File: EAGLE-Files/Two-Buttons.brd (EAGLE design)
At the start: 25.4 x 40.3 mm, 10 parts

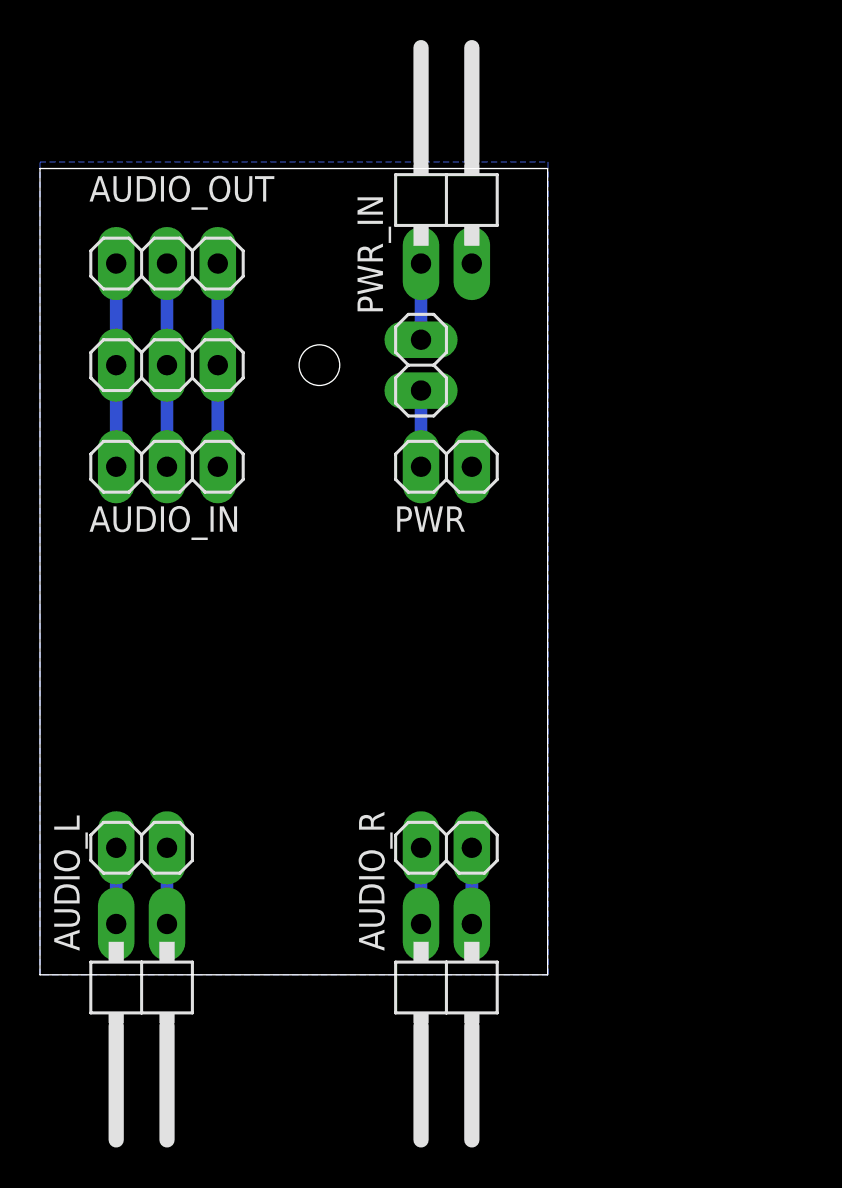
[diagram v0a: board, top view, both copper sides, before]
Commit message: Updated all boards for JLCPCB order
Also added the controller boards and schematics back
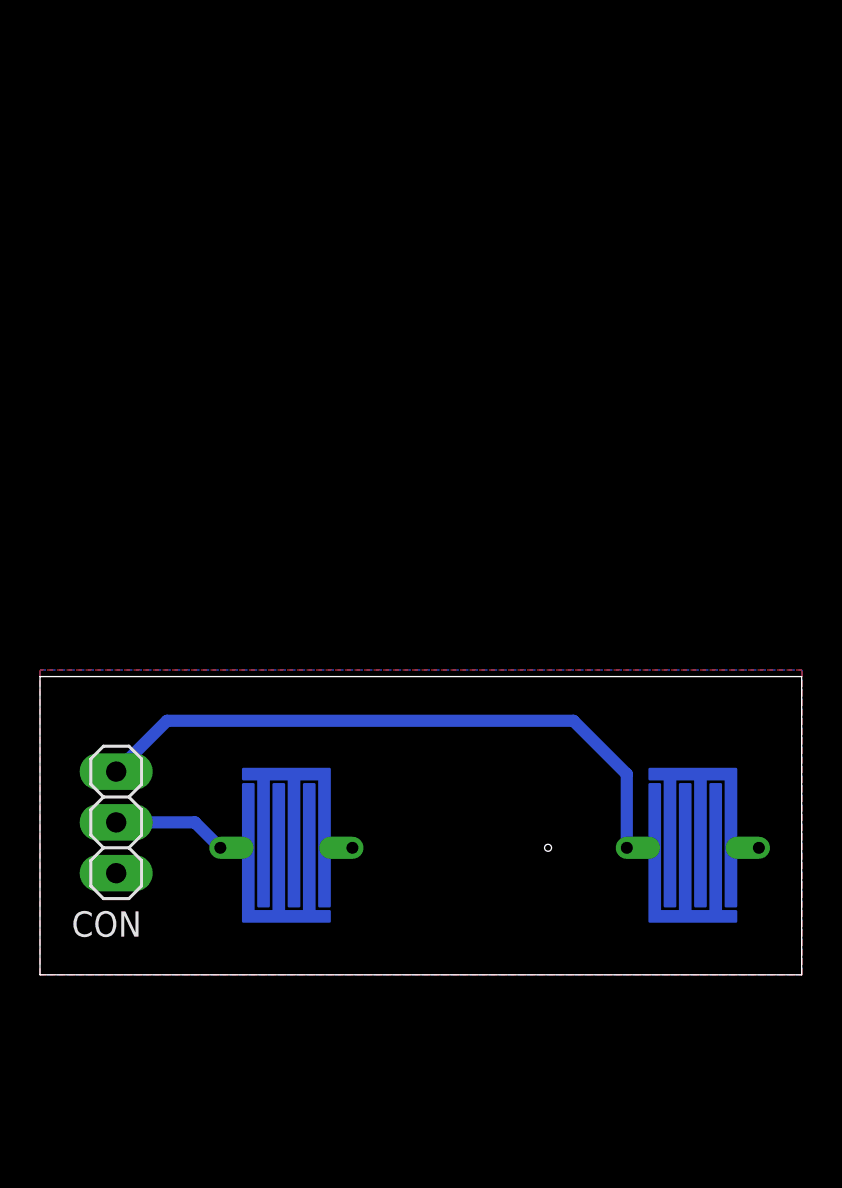
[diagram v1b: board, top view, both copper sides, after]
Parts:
- removed AUDIO_CONNECTOR, AUDIO_IN, AUDIO_OUT: (no value), pinhead:1X03
- removed AUDIO_L, AUDIO_R, PWR, SWITCH: (no value), pinhead:1X02
- removed AUDIO_L_OUT, AUDIO_R_OUT, PWR_IN: (no value), pinhead:1X02/90
- added BTN1, BTN2: BTN_5MM_LONG, surfacebuttons:BTN_5MM_LONG
- added CON: (no value), pinhead:1X03
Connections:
- removed net +5V: PWR.1, SWITCH.1
- removed net N$1: AUDIO_CONNECTOR.3, AUDIO_IN.1, AUDIO_OUT.1
- removed net N$2: AUDIO_CONNECTOR.2, AUDIO_IN.2, AUDIO_OUT.2
- removed net N$3: AUDIO_CONNECTOR.1, AUDIO_IN.3, AUDIO_OUT.3
- removed net N$4: AUDIO_L.1, AUDIO_L_OUT.2
- removed net N$5: AUDIO_L.2, AUDIO_L_OUT.1
- removed net N$6: AUDIO_R.2, AUDIO_R_OUT.1
- removed net N$7: AUDIO_R.1, AUDIO_R_OUT.2
- removed net N$8: PWR_IN.1, SWITCH.2
- new net B1: BTN1.P$1, CON.2
- new net B2: BTN2.P$1, CON.3
- net GND: now also BTN1.P$2, BTN2.P$2, CON.1; no longer PWR.2, PWR_IN.2
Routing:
- net B2: track 0.00 -> 31.4 mm
- net N$3: track 10.2 -> 0.00 mm
- net N$2: track 10.2 -> 0.00 mm
- net N$1: track 10.2 -> 0.00 mm
- net B1: track 0.00 -> 5.73 mm
- net N$8: track 3.81 -> 0.00 mm
- net +5V: track 3.81 -> 0.00 mm
- net N$7: track 3.81 -> 0.00 mm
- net N$6: track 3.81 -> 0.00 mm
- net N$5: track 3.81 -> 0.00 mm
- net N$4: track 3.81 -> 0.00 mm
- added copper zone on layer 1, net GND
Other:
- board size 25.4 x 40.3 mm -> 38.1 x 14.9 mm
